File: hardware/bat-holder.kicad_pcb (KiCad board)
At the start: 2 copper layers, 85 x 56 mm, 27 parts, among them J101 BAT_1049P, K101 BAT, K102 NTC, U101 AAT4685-1, U102 AAT4685-1

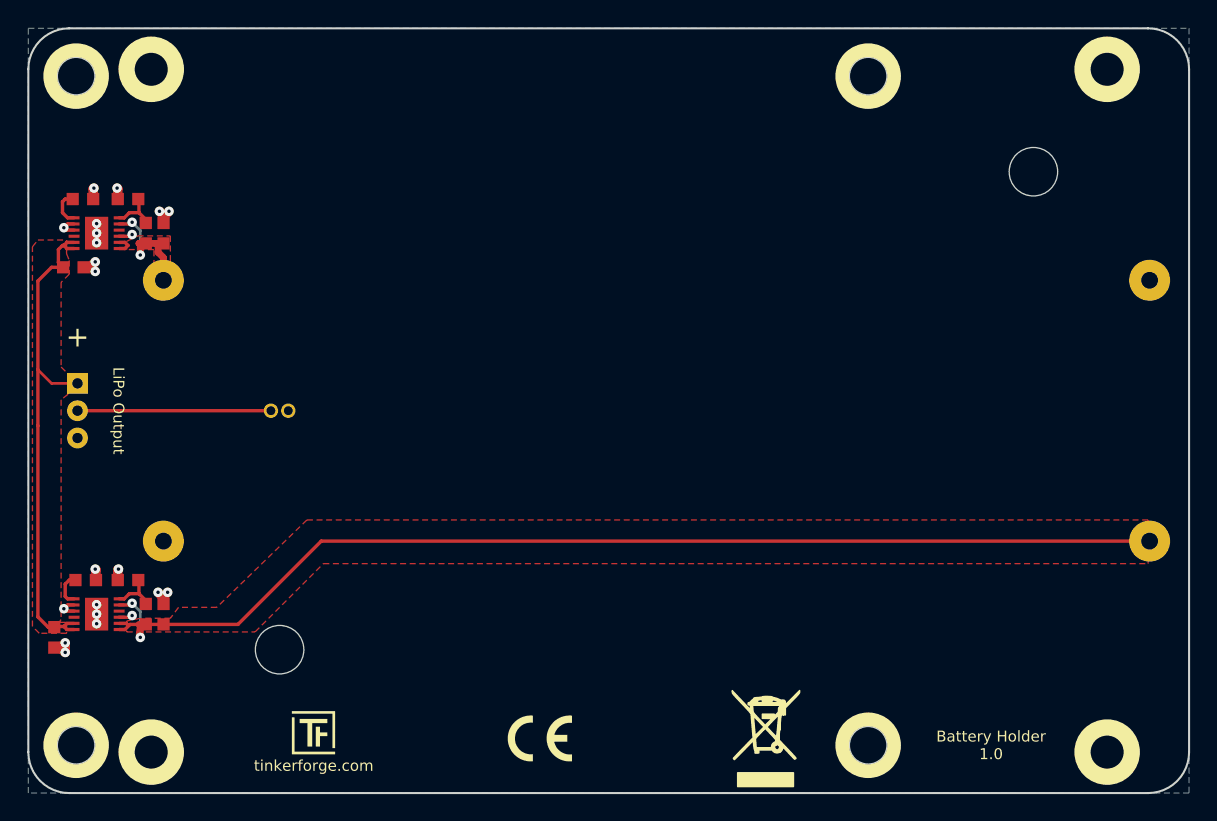
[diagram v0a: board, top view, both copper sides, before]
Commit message: change to ap9211 battery protection ic
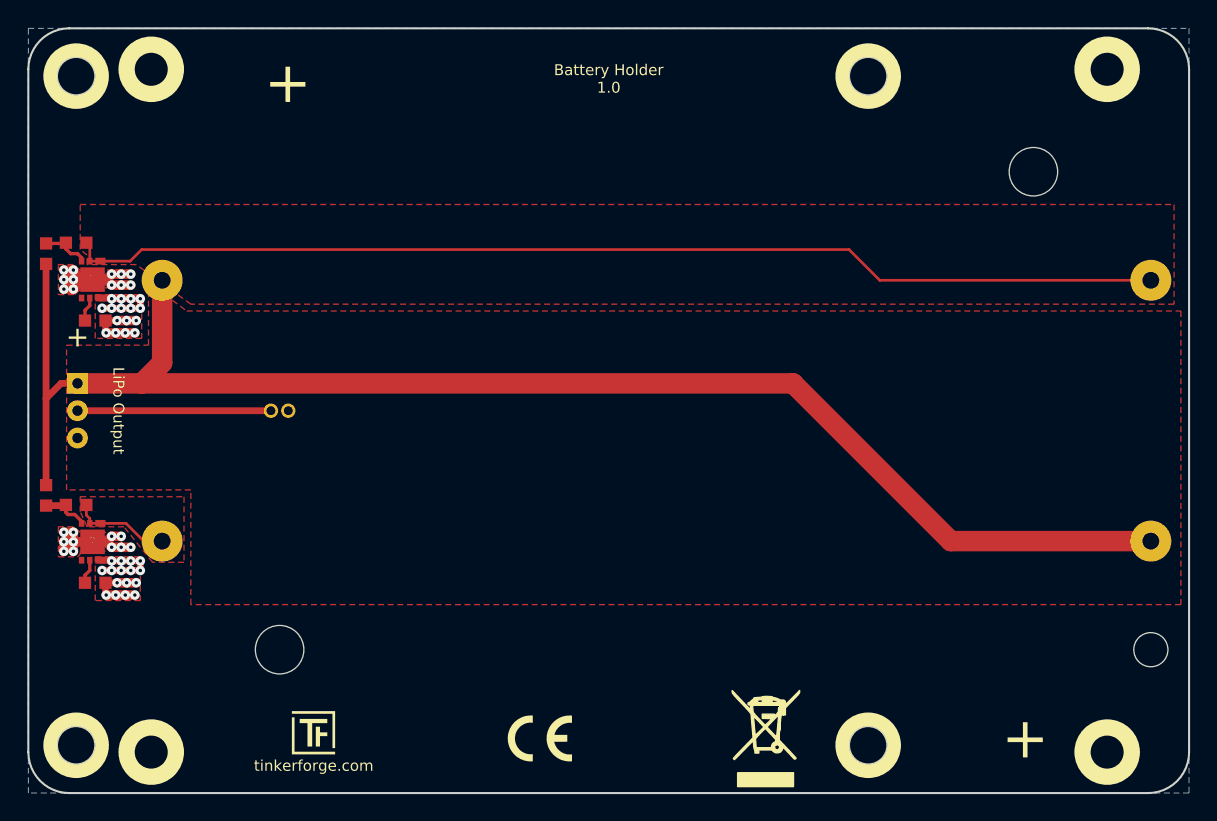
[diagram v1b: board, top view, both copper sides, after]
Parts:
- removed C103, C104: 1µF, C0603F
- removed R105, R106: 16.5k, R0603F
- added P101: C, TSTPT, F.Cu at (77.7, 94.4)
- added P102: C, TSTPT, F.Cu at (77.7, 113.6)
- C101, C102: value 1µF -> 100nF
- R101: value 340k -> 330
- R102: value 100k -> 330
- R103: value 340k -> 2.7k
- R104: value 100k -> 2.7k
- U101, U102: value AAT4685-1 -> AP9211; footprint TDFN33-12 -> DFN2030-6
- moved R102 22.5 mm to (74.3, 110.2), turned to 90 degrees
- moved R103 21.8 mm to (77.9, 97.4), turned to 180 degrees
- moved C102 10.2 mm to (76.5, 110.9), turned to 0 degrees
- moved R101 7.45 mm to (74.3, 92.5)
- moved C101 6.44 mm to (76.5, 91.7), turned to 0 degrees
- moved U102 5.31 mm to (77.7, 113.6), turned to 180 degrees
- moved U101 3.41 mm to (77.7, 94.4), turned to 180 degrees
- moved R104 2.41 mm to (77.9, 116.6), turned to 180 degrees
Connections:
- C101 pad 1: BAT1 -> Net-(C101-Pad1)
- C101 pad 2: GND -> GBAT1
- C102 pad 1: BAT2 -> Net-(C102-Pad1)
- C102 pad 2: GND -> GBAT2
- J101 pad 2: GND -> GBAT2
- J101 pad 3: BAT2 -> BAT1
- J101 pad 4: GND -> GBAT1
- K101 pad 1: OUT -> BAT1
- R101 pad 1: Net-(R101-Pad1) -> Net-(C101-Pad1)
- R102 pad 1: GND -> Net-(C102-Pad1)
- R102 pad 2: Net-(R101-Pad1) -> BAT1
- R103 pad 1: Net-(R103-Pad1) -> GND
- R103 pad 2: BAT2 -> Net-(R103-Pad2)
- R104 pad 2: Net-(R103-Pad1) -> Net-(R104-Pad2)
- U101 pad 1: Net-(R105-Pad2) -> GBAT1
- U101 pad 2: GND -> GBAT1
- U101 pad 3: GND -> Net-(C101-Pad1)
- U101 pad 5: OUT -> Net-(R103-Pad2)
- U101 pad 6: OUT -> GND
- U101 pad EP: GND -> EP1
- U102 pad 1: Net-(R106-Pad2) -> GBAT2
- U102 pad 2: GND -> GBAT2
- U102 pad 3: GND -> Net-(C102-Pad1)
- U102 pad 5: OUT -> Net-(R104-Pad2)
- U102 pad 6: OUT -> GND
- U102 pad EP: GND -> EP2
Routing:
- net BAT1: track 11.4 -> 110.5 mm, vias 2 -> 0
- net BAT2: track 84.6 -> 0.00 mm, vias 2 -> 0
- net GBAT1: track 0.00 -> 80.4 mm
- net OUT: track 37.8 -> 0.00 mm
- net EP1: track 0.00 -> 11.9 mm, vias 0 -> 12
- net EP2: track 0.00 -> 9.13 mm, vias 0 -> 11
- net GBAT2: track 0.00 -> 7.29 mm
- net Net-(C102-Pad1): track 0.00 -> 3.59 mm
- net Net-(C101-Pad1): track 0.00 -> 3.59 mm
- net Net-(R103-Pad1): track 3.58 -> 0.00 mm
- net Net-(R101-Pad1): track 3.58 -> 0.00 mm
- net GND: track 20.0 -> 23.4 mm, vias 22 -> 32
- net Net-(R105-Pad2): track 2.64 -> 0.00 mm
- net Net-(R106-Pad2): track 2.50 -> 0.00 mm
- net Net-(R103-Pad2): track 0.00 -> 1.79 mm
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- added copper zone on F.Cu, net EP1
- added copper zone on F.Cu, net EP2
- added copper zone on F.Cu, net GBAT1
- added copper zone on F.Cu, net GBAT2
- added copper zone on F.Cu, net GND
- removed copper zone on F.Cu, net BAT2
- removed copper zone on F.Cu, net OUT

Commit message: add hint, add datasheet
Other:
- board text added: "Check Connector"
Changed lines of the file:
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@@
   (general
     (thickness 1.6)
-    (drawings 23)
+    (drawings 24)
     (tracks 165)
     (zones 0)
@@
       (net 11 EP2))
   )
+  (gr_text "Check Connector" (at 54.6 110.7) (layer Dwgs.User)
+    (effects (font (size 5 5) (thickness 0.3)))
+  )
   (gr_text + (at 146 128) (layer F.SilkS)

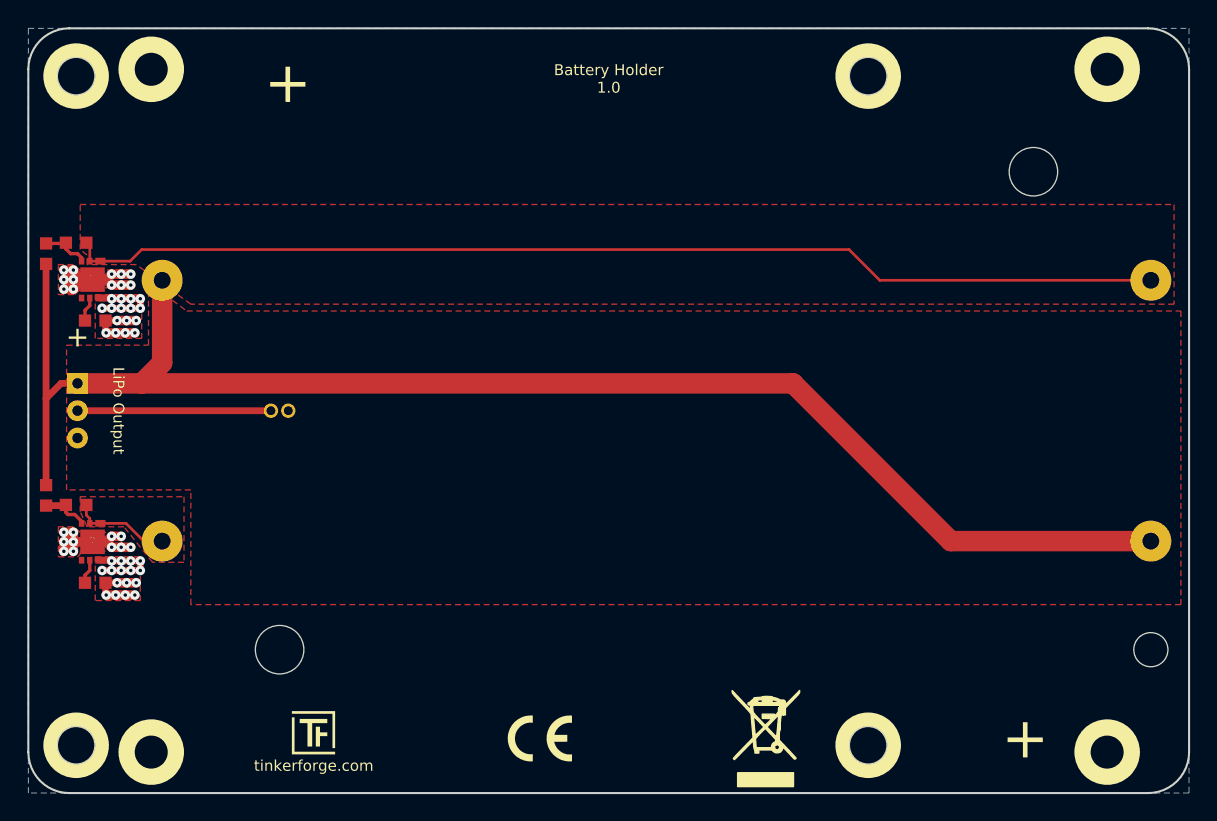
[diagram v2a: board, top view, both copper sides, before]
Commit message: change reverse polarity protection of batteries
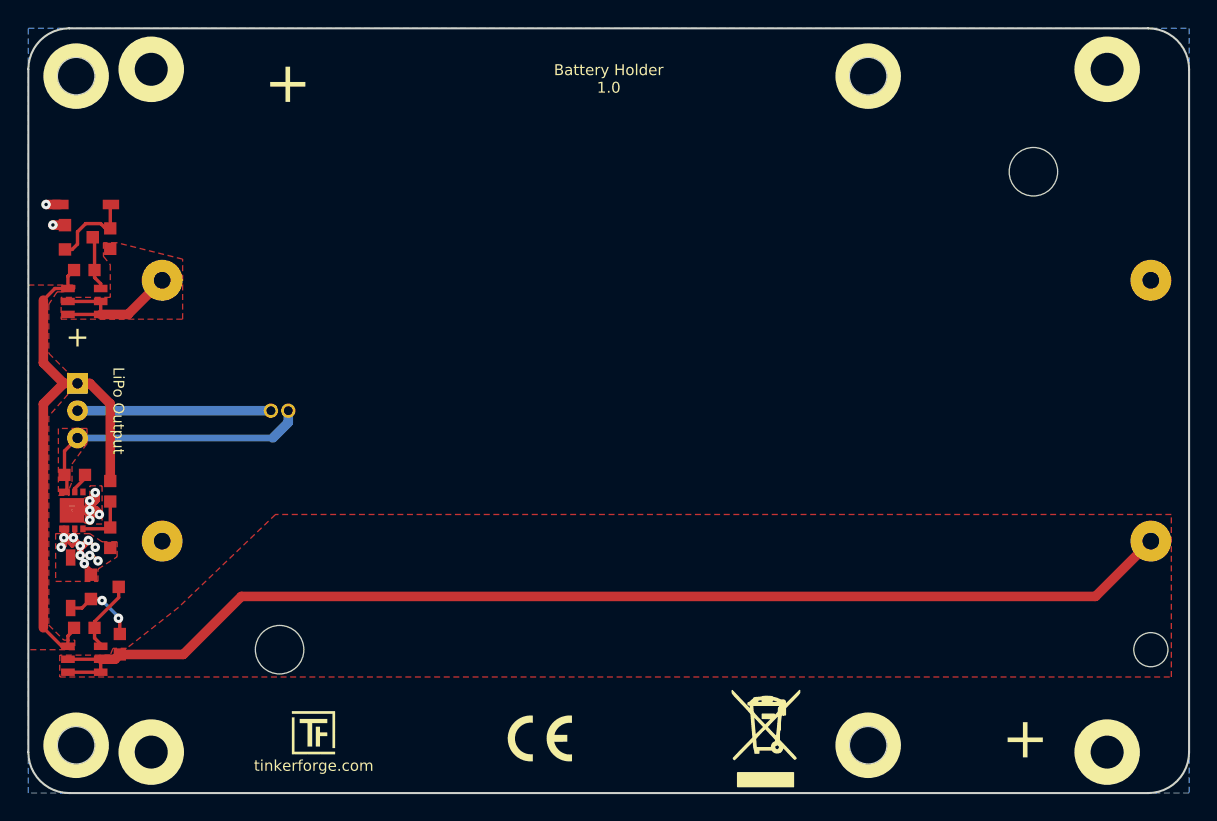
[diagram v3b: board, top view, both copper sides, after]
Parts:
- removed C102: 100nF, C0603F
- removed P102: C, TSTPT
- removed U102: AP9211, DFN2030-6
- added D101: LL4148, SOD-123, F.Cu at (77.2, 88.9)
- added D102: LL4148, SOD-123, F.Cu at (76.1, 116.6)
- added Q101: NPN, SOT23EBC, F.Cu at (76.7, 91.3)
- added Q102: NPN, SOT23EBC, F.Cu at (78.6, 116.9)
- added Q103: DMP2035UVTQ, SOT26GDS, F.Cu at (77.1, 96.0)
- added Q104: DMP2035UVTQ, SOT26GDS, F.Cu at (77.1, 122.2)
- added R105: 330, R0603F, F.Cu at (79.0, 109.9)
- added R106: 2.7k, R0603F, F.Cu at (76.4, 108.7)
- R101, R102: value 330 -> 10k
- R103, R104: value 2.7k -> 10k
- moved C101 21.7 mm to (79.0, 113.3), turned to 270 degrees
- moved P101 17.0 mm to (76.2, 111.3)
- moved U101 17.0 mm to (76.2, 111.3), turned to 0 degrees
- moved R102 12.2 mm to (79.7, 121.1), turned to 270 degrees
- moved R101 4.83 mm to (79.0, 91.4)
- moved R103 3.79 mm to (77.1, 93.7)
- moved R104 3.40 mm to (77.1, 119.9)
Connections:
- C101 pad 2: GBAT1 -> GBAT
- J101 pad 1: BAT1 -> VBAT1
- J101 pad 2: GBAT2 -> GBAT
- J101 pad 3: BAT1 -> VBAT2
- J101 pad 4: GBAT1 -> GBAT
- K101 pad 1: BAT1 -> OUT
- R101 pad 1: Net-(C101-Pad1) -> Net-(D101-Pad2)
- R101 pad 2: BAT1 -> VBAT1
- R102 pad 2: BAT1 -> VBAT2
- R103 pad 1: GND -> Net-(Q101-PadC)
- R103 pad 2: Net-(R103-Pad2) -> OUT
- R104 pad 1: GND -> Net-(Q102-PadC)
- R104 pad 2: Net-(R104-Pad2) -> OUT
- U101 pad 1: GBAT1 -> GBAT
- U101 pad 2: GBAT1 -> GBAT
- U101 pad 5: Net-(R103-Pad2) -> Net-(R106-Pad2)
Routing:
- net BAT1: track 110.5 -> 0.00 mm
- net VBAT2: track 0.00 -> 86.2 mm
- net GBAT1: track 80.4 -> 0.00 mm
- net OUT: track 0.00 -> 42.5 mm
- net GBAT: track 0.00 -> 12.3 mm, vias 0 -> 12
- net VBAT1: track 0.00 -> 11.3 mm
- net EP2: track 9.13 -> 0.00 mm, vias 11 -> 0
- net EP1: track 11.9 -> 4.47 mm, vias 12 -> 5
- net GBAT2: track 7.29 -> 0.00 mm
- net Net-(D101-Pad2): track 0.00 -> 6.54 mm
- net Net-(Q102-PadC): track 0.00 -> 5.27 mm
- net Net-(Q101-PadC): track 0.00 -> 3.99 mm
- net GND: track 23.4 -> 21.3 mm, vias 32 -> 0
- net Net-(D102-Pad2): track 3.59 -> 5.61 mm, vias 0 -> 2
- net Net-(R103-Pad2): track 1.79 -> 0.00 mm
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- added copper zone on B.Cu, net GBAT
- added copper zone on F.Cu, net GBAT
- added copper zone on F.Cu, net OUT
- added copper zone on F.Cu, net VBAT1
- added copper zone on F.Cu, net VBAT2
- removed copper zone on F.Cu, net BAT1
- removed copper zone on F.Cu, net EP2
- removed copper zone on F.Cu, net GBAT1
- removed copper zone on F.Cu, net GBAT2
- removed copper zone on B.Cu, net GND
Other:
- board text added: "Copyright Tinkerforge GmbH 2018. This documentation describes Open Hardware and is licensed under the CERN OHL v. 1.1. You may redistribute and modify this documentation under the terms of the CERN OHL v.1.1. (http://ohwr.org/cernohl). This documentation is distributed WITHOUT ANY EXPRESS OR IMPLIED WARRANTY, INCLUDING OF MERCHANTABILITY, SATISFACTORY QUALITY AND FITNESS FOR A PARTICULAR PURPOSE.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"
- board text removed: "Check Connector"
- board text removed: "Copyright Tinkerforge GmbH 2015. This documentation describes Open Hardware and is licensed under the CERN OHL v. 1.1. You may redistribute and modify this documentation under the terms of the CERN OHL v.1.1. (http://ohwr.org/cernohl). This documentation is distributed WITHOUT ANY EXPRESS OR IMPLIED WARRANTY, INCLUDING OF MERCHANTABILITY, SATISFACTORY QUALITY AND FITNESS FOR A PARTICULAR PURPOSE.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"
